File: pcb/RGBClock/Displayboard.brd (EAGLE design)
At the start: 70 x 58.5 mm, 66 parts, among them U1 LP3878MR-ADJ, U10 MCP23017SO, U2 P82B96DR, U3 P82B96DR, U4 PCA9685PW, U5 TPS71533DCKR, U6 ZXLD1362ET5TA, U7 74HCT1G14GW, U8 74HCT1G86GW, U9 TPA0172-HTSSOP24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

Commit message: Adding analog power and light sensor
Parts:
- added R27: A1-1, resistor:R0402
- added R28: A1-0, resistor:R0402
- added U11: TSL2561, MyComponents:TMB-6
- moved R4 8.64 mm to (26.2, 32.8), turned to 180 degrees
- moved R3 8.38 mm to (26.2, 36.3), turned to 180 degrees
- moved C7 1.14 mm to (40.1, 26.4)
- moved C1 1.05 mm to (17.5, 53.6), turned to 90 degrees
- moved C5 1.02 mm to (32.5, 26.4), turned to 270 degrees
- moved U5 1.02 mm to (36.3, 26.4)
- moved C14 0.52 mm to (39.9, 4.32)
- moved C12 0.51 mm to (19.1, 4.32)
- moved C16 0.40 mm to (39.9, 7.37)
- moved C10 0.38 mm to (19.1, 7.37)
- moved C17 0.28 mm to (39.9, 10.4)
- moved R13 0.28 mm to (22.6, 15.7)
- moved R11 0.28 mm to (22.6, 2.03)
- moved C9 0.25 mm to (19.1, 10.4)
- moved C18 0.18 mm to (39.9, 13.5)
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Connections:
- new net N$34: R27.1, R28.2, U11.2
- net +3V3: now also R27.2, U11.1
- net GND: now also R28.1, U11.3
- net N$7: now also U11.6
- net N$9: now also U11.4
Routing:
- net GND: track 375.3 -> 0.00 mm, vias 5 -> 0
- net +5V: track 272.3 -> 0.00 mm, vias 8 -> 0
- net SDA: track 126.1 -> 0.00 mm, vias 4 -> 0
- net SCL: track 85.1 -> 0.00 mm, vias 3 -> 0
- net VCC: track 60.0 -> 0.00 mm
- net +3V3: track 55.9 -> 0.00 mm, vias 2 -> 0
- net N$22: track 44.3 -> 0.00 mm
- net D2: track 42.4 -> 0.00 mm
- net N$12: track 37.7 -> 0.00 mm, vias 1 -> 0
- net N$2: track 35.3 -> 0.00 mm
- net N$8: track 25.8 -> 0.00 mm
- net N$11: track 25.7 -> 0.00 mm, vias 1 -> 0
- net N$49: track 24.8 -> 0.00 mm
- net D0: track 23.9 -> 0.00 mm, vias 1 -> 0
- net N$3: track 23.2 -> 0.00 mm
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- removed copper zone on layer 1, net GND

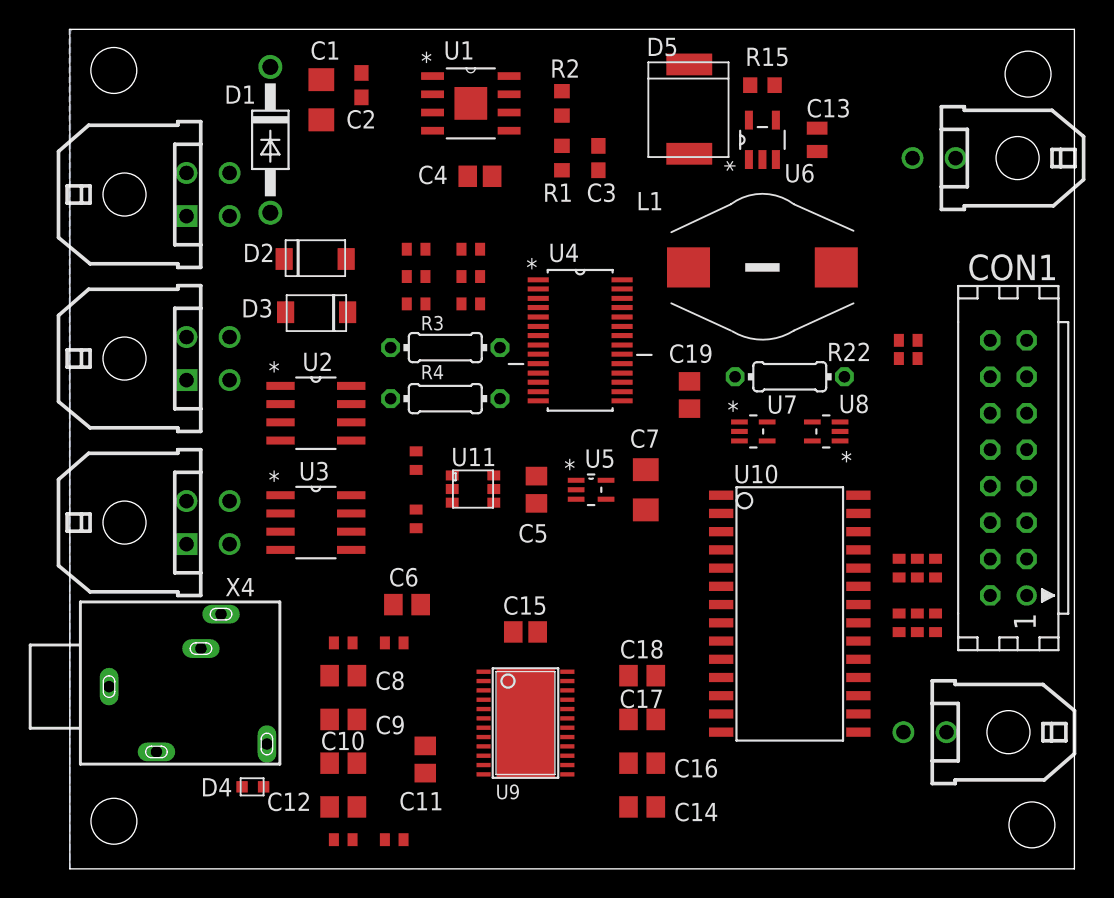
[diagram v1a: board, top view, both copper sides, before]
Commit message: updating component packages
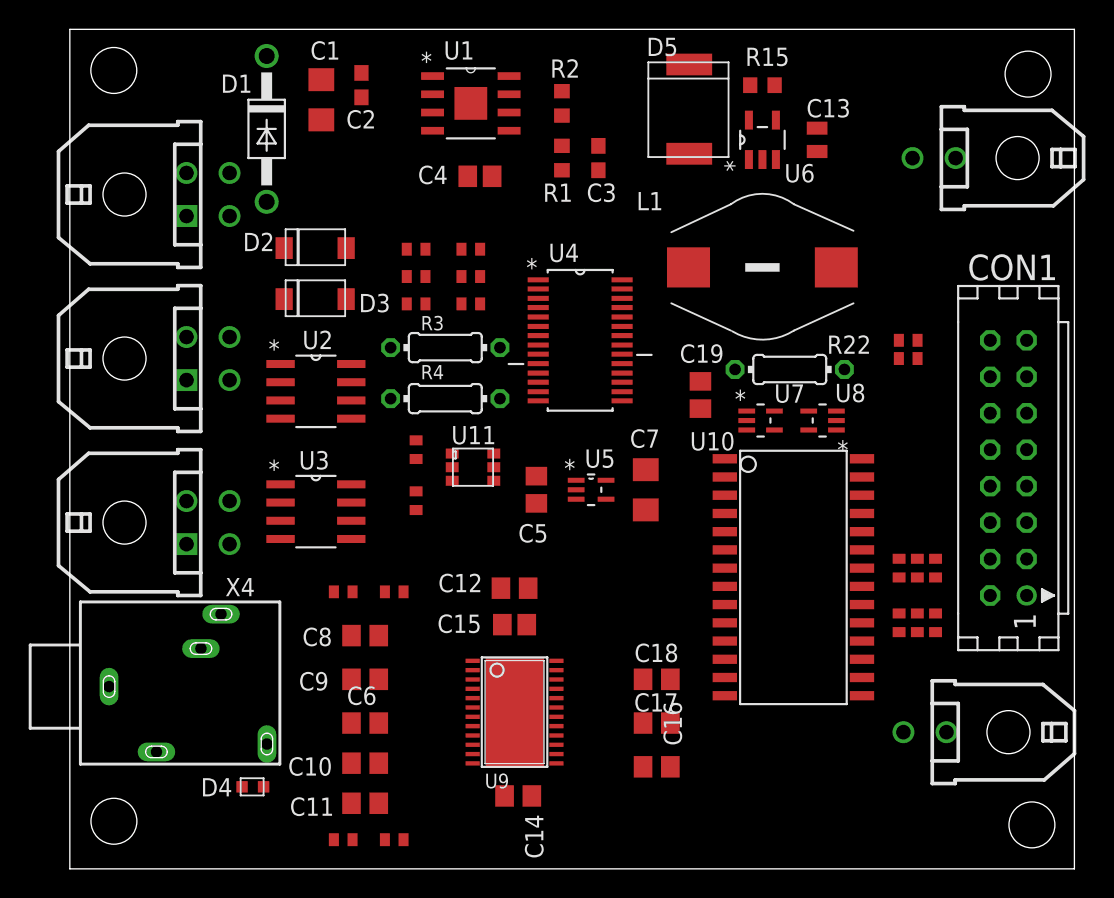
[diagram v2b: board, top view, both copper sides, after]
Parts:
- moved C12 19.4 mm to (31.0, 19.6)
- moved C6 8.76 mm to (20.6, 10.2)
- moved C14 8.67 mm to (31.2, 5.08)
- moved C11 5.18 mm to (20.6, 4.57), turned to 0 degrees
- moved R13 3.56 mm to (22.6, 19.3)
- moved R14 3.56 mm to (19.1, 19.3)
- moved C8 3.18 mm to (20.6, 16.3)
- moved C9 3.18 mm to (20.6, 13.2)
- moved U10 2.55 mm to (50.4, 21.0)
- moved C10 1.52 mm to (20.6, 7.37)
- moved U11 1.52 mm to (28.2, 27.9)
- moved U2 1.52 mm to (17.1, 33.3)
- moved R28 1.27 mm to (24.1, 25.7)
- moved U9 1.08 mm to (31.0, 10.9)
- moved C16 1.05 mm to (40.9, 7.11)
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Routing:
- removed copper zone on layer 16, net GND

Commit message: Main and Display updated
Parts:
- C1, C7: device rcl:C1206 -> rcl:C0805
- C15, C4: device rcl:C2012 -> rcl:C0805
- C2, C3: device rcl:C1608 -> rcl:C0805
- moved D4 14.0 mm to (12.2, 19.7), turned to 0 degrees
- moved C2 1.02 mm to (20.3, 53.6)
- moved C4 0.92 mm to (28.1, 49.0)
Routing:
- net GND: track 0.00 -> 400.1 mm, vias 0 -> 3
- net +5V: track 0.00 -> 266.1 mm, vias 0 -> 8
- net SDA: track 0.00 -> 140.8 mm, vias 0 -> 3
- net SCL: track 0.00 -> 80.3 mm, vias 0 -> 3
- net VCC: track 0.00 -> 59.4 mm
- net +3V3: track 0.00 -> 58.5 mm
- net N$7: track 0.00 -> 48.0 mm
- net N$22: track 0.00 -> 46.5 mm, vias 0 -> 1
- net N$9: track 0.00 -> 44.6 mm
- net N$12: track 0.00 -> 39.5 mm, vias 0 -> 1
- net D0: track 0.00 -> 35.6 mm
- net N$8: track 0.00 -> 31.5 mm
- net N$2: track 0.00 -> 29.9 mm
- net N$11: track 0.00 -> 27.6 mm, vias 0 -> 1
- net RW: track 0.00 -> 23.2 mm, vias 0 -> 1
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- added copper zone on layer 1, net GND
- added copper zone on layer 16, net GND

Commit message: Ready
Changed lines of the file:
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@@
 <layer number="27" name="tValues" color="7" fill="1" visible="yes" active="yes"/>
 <layer number="28" name="bValues" color="7" fill="1" visible="yes" active="yes"/>
-<layer number="29" name="tStop" color="7" fill="3" visible="no" active="yes"/>
+<layer number="29" name="tStop" color="7" fill="3" visible="yes" active="yes"/>
 <layer number="30" name="bStop" color="7" fill="6" visible="no" active="yes"/>
 <layer number="31" name="tCream" color="7" fill="4" visible="no" active="yes"/>
@@
 </element>
 <element name="D3" library="MyComponents" package="DO-221AC" value="SMA6F" x="17.145" y="39.751" smashed="yes">
-<attribute name="NAME" x="12.263" y="38.537" size="1.27" layer="21"/>
+<attribute name="NAME" x="11.755" y="38.537" size="1.27" layer="21"/>
 </element>
 <element name="D2" library="MyComponents" package="DO-221AC" value="SMA6F" x="17.145" y="43.307" smashed="yes">
-<attribute name="NAME" x="12.311" y="42.283" size="1.27" layer="21"/>
+<attribute name="NAME" x="11.549" y="42.283" size="1.27" layer="21"/>
 </element>
 <element name="U10" library="microchip" package="SO28W" value="MCP23017SO" x="50.419" y="20.955" smashed="yes" rot="R270">
@@
 </element>
 <element name="R18" library="resistor" package="R0402" value="A1-1" x="59.055" y="17.145" smashed="yes" rot="R270">
-<attribute name="VALUE" x="58.523" y="15.28" size="0.8128" layer="27" rot="R270"/>
+<attribute name="VALUE" x="58.777" y="14.772" size="0.8128" layer="27" rot="R270"/>
 </element>
 <element name="R19" library="resistor" package="R0402" value="A1-0" x="59.055" y="20.955" smashed="yes" rot="R270">
@@
 </element>
 <element name="R16" library="resistor" package="R0402" value="A0-1" x="60.325" y="17.145" smashed="yes" rot="R270">
-<attribute name="VALUE" x="59.793" y="15.28" size="0.8128" layer="27" rot="R270"/>
+<attribute name="VALUE" x="60.555" y="15.788" size="0.8128" layer="27" rot="R270"/>
 </element>
 <element name="R17" library="resistor" package="R0402" value="A0-0" x="60.325" y="20.955" smashed="yes" rot="R270">
@@
 </element>
 <element name="R20" library="resistor" package="R0402" value="A2-1" x="57.785" y="17.145" smashed="yes" rot="R270">
-<attribute name="VALUE" x="57.253" y="15.28" size="0.8128" layer="27" rot="R270"/>
+<attribute name="VALUE" x="57.253" y="14.01" size="0.8128" layer="27" rot="R270"/>
 </element>
 <element name="R21" library="resistor" package="R0402" value="A2-0" x="57.785" y="20.955" smashed="yes" rot="R270">
@@
 </element>
 <element name="R9" library="resistor" package="R0402" value="A0-1" x="27.94" y="43.18" smashed="yes">
-<attribute name="VALUE" x="29.7034" y="42.902" size="0.8128" layer="27"/>
+<attribute name="VALUE" x="29.7034" y="43.918" size="0.8128" layer="27"/>
 </element>
 <element name="R10" library="resistor" package="R0402" value="A0-0" x="24.13" y="43.18" smashed="yes">
@@
 </element>
 <element name="R7" library="resistor" package="R0402" value="A1-1" x="27.94" y="41.275" smashed="yes">
-<attribute name="VALUE" x="29.7542" y="40.8954" size="0.8128" layer="27"/>
+<attribute name="VALUE" x="29.7542" y="41.9114" size="0.8128" layer="27"/>
 </element>
 <element name="R5" library="resistor" package="R0402" value="A2-1" x="27.94" y="39.37" smashed="yes">
-<attribute name="VALUE" x="29.805" y="38.9904" size="0.8128" layer="27"/>
+<attribute name="VALUE" x="29.297" y="37.9744" size="0.8128" layer="27"/>
 </element>
 <element name="R8" library="resistor" package="R0402" value="A1-0" x="24.13" y="41.275" smashed="yes">
@@
 </element>
 <element name="C19" library="rcl" package="C0805" value="22n" x="43.942" y="33.02" smashed="yes" rot="R90">
-<attribute name="NAME" x="45.584" y="36.538" size="1.27" layer="25" rot="R180"/>
+<attribute name="NAME" x="42.79" y="34.76" size="1.27" layer="25" rot="R180"/>
 </element>
 <element name="U11" library="MyComponents" package="TMB-6" value="TSL2561" x="28.194" y="27.94" smashed="yes">
